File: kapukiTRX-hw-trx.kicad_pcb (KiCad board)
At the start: 4 copper layers, 45.7 x 27.9 mm, 97 parts, among them J1 GPS, J10 Conn_01x01, J11 Conn_01x01, J12 Conn_01x01, J13 Conn_01x01, J14 Conn_01x01, J15 Conn_01x01, J16 Conn_01x01, J17 Conn_01x01, J18 Conn_01x01, J19 GND for the Servo connectors, J2 SWD, J20 CAN, J21 Conn_01x01, J22 Conn_01x01, J3 Conn_01x01, J4 Conn_01x01, J5 Conn_01x01, J6 Conn_01x01, J7 Conn_01x01, J8 Conn_01x01, J9 Conn_01x01, U1 STM32G474VE, U2 LP38693-3.3, U3 TXB0108PWR, U4 LP38693-5.0, U5 MCP2562-E-MF, U6 LP38693SD-3.3, U7 BNO055, U8 BMP388, Y1 16MHz, Y2 32.768kHz

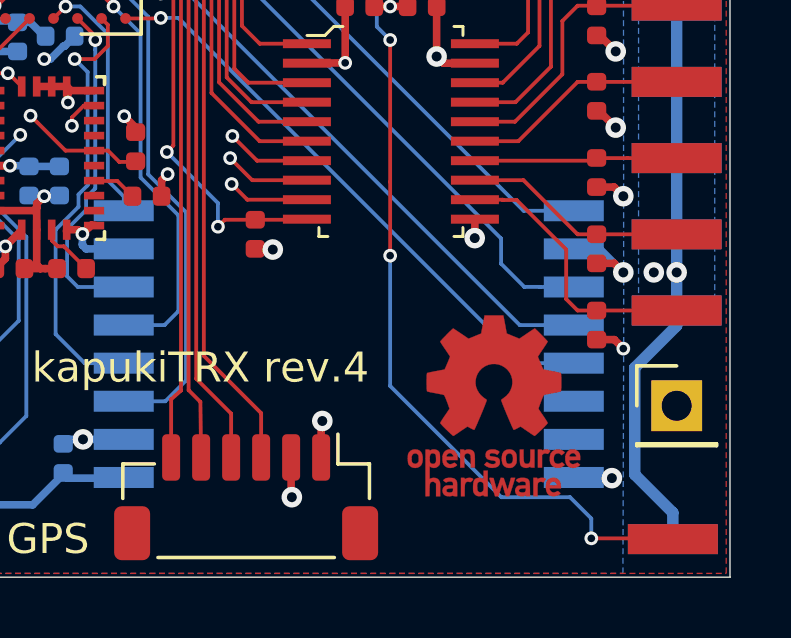
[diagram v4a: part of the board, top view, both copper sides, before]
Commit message: Add pull-up for uart
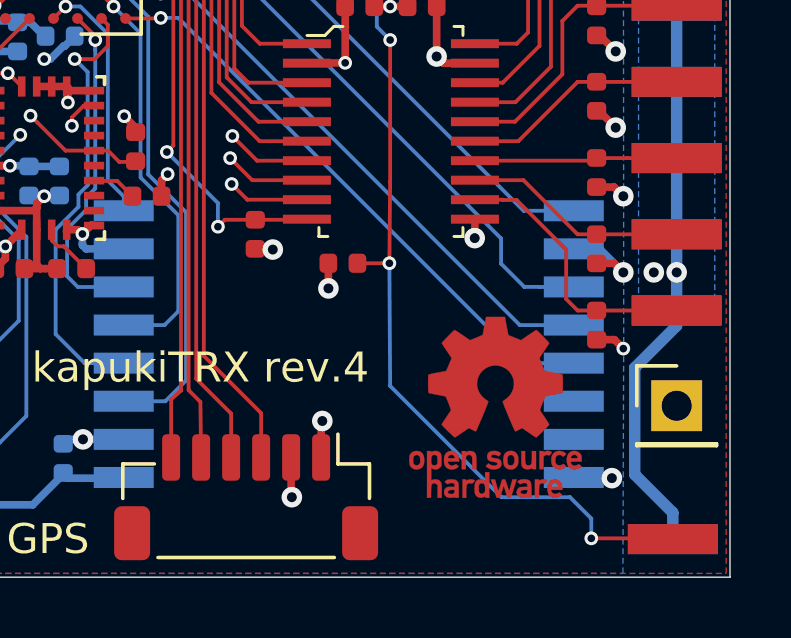
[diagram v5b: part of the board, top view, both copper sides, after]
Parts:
- added R19: 4k7, Resistor_SMD:R_0402_1005Metric, F.Cu at (204.3, 111.5)
- R16: value 10k -> 5k97
- R17: value 10k -> 2k4
- R6: value 1k -> 470
- R9: value 120R -> 120
- moved REF** 0.07 mm to (209.3, 116.3)
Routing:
- net /RXTX: track 42.2 -> 43.3 mm
- net /VCCCPU: track 49.8 -> 50.6 mm, vias 18 -> 19
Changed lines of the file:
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@@
-(kicad_pcb (version 20171130) (host pcbnew "(5.1.4)-1")
+(kicad_pcb (version 20171130) (host pcbnew "(5.1.4-0-10_14)")
   (general
     (thickness 1.6)
     (drawings 17)
-    (tracks 1089)
+    (tracks 1094)
     (zones 0)
-    (modules 97)
+    (modules 98)
     (nets 129)
   )
@@
   (layers
     (0 F.Cu signal)
-    (1 In1.Cu signal)
-    (2 In2.Cu signal)
-    (31 B.Cu signal)
+    (1 In1.Cu signal hide)
+    (2 In2.Cu signal hide)
+    (31 B.Cu signal hide)
     (32 B.Adhes user hide)
     (33 F.Adhes user hide)
@@
   )
   (module Symbol:OSHW-Logo_5.7x6mm_Copper (layer F.Cu)
-    (at 209.296 116.205)
+    (at 209.3468 116.2558)
     (descr "Open Source Hardware Logo")
     (tags "Logo OSHW")
@@
       (xy -1.971615 1.454739) (xy -1.908759 1.469184)) (layer F.Cu) (width 0.01))
   )
+  (module Resistor_SMD:R_0402_1005Metric (layer F.Cu)
+    (at 204.2668 111.4552 180)
+    (descr "Resistor SMD 0402 (1005 Metric), square (rectangular) end terminal, IPC_7351 nominal, (Body size source: http://www.tortai-tech.com/upload/download/2011102023233369053.pdf), generated with kicad-footprint-generator")
+    (tags resistor)
+    (attr smd)
+    (fp_text reference R19 (at 0 -1.17) (layer F.SilkS) hide
+      (effects (font (size 1 1) (thickness 0.15)))
+    )
+    (fp_text value 4k7 (at 0 1.17) (layer F.Fab)
+      (effects (font (size 1 1) (thickness 0.15)))
+    )
+    (fp_text user %R (at 0 0) (layer F.Fab)
+      (effects (font (size 0.25 0.25) (thickness 0.04)))
+    )
+    (fp_line (start 0.93 0.47) (end -0.93 0.47) (layer F.CrtYd) (width 0.05))
+    (fp_line (start 0.93 -0.47) (end 0.93 0.47) (layer F.CrtYd) (width 0.05))
+    (fp_line (start -0.93 -0.47) (end 0.93 -0.47) (layer F.CrtYd) (width 0.05))
+    (fp_line (start -0.93 0.47) (end -0.93 -0.47) (layer F.CrtYd) (width 0.05))
+    (fp_line (start 0.5 0.25) (end -0.5 0.25) (layer F.Fab) (width 0.1))
+    (fp_line (start 0.5 -0.25) (end 0.5 0.25) (layer F.Fab) (width 0.1))
+    (fp_line (start -0.5 -0.25) (end 0.5 -0.25) (layer F.Fab) (width 0.1))
+    (fp_line (start -0.5 0.25) (end -0.5 -0.25) (layer F.Fab) (width 0.1))
+    (pad 2 smd roundrect (at 0.485 0 180) (size 0.59 0.64) (layers F.Cu F.Paste F.Mask) (roundrect_rratio 0.25)
+      (net 25 /VCCCPU))
+    (pad 1 smd roundrect (at -0.485 0 180) (size 0.59 0.64) (layers F.Cu F.Paste F.Mask) (roundrect_rratio 0.25)
+      (net 122 /RXTX))
+    (model ${KISYS3DMOD}/Resistor_SMD.3dshapes/R_0402_1005Metric.wrl
+      (at (xyz 0 0 0))
+      (scale (xyz 1 1 1))
+      (rotate (xyz 0 0 0))
+    )
+  )
   (module Resistor_SMD:R_0402_1005Metric (layer B.Cu)
     (at 193.167 96.2152 180)
@@
       (effects (font (size 1 1) (thickness 0.15)))
     )
-    (fp_text value 10k (at 0 1.17) (layer F.Fab)
+    (fp_text value 2k4 (at 0 1.17) (layer F.Fab)
       (effects (font (size 1 1) (thickness 0.15)))
     )
@@
       (effects (font (size 1 1) (thickness 0.15)))
     )
-    (fp_text value 10k (at 0 1.17) (layer F.Fab)
+    (fp_text value 5k97 (at 0 1.17) (layer F.Fab)
       (effects (font (size 1 1) (thickness 0.15)))
     )
@@
       (effects (font (size 1 1) (thickness 0.15)))
     )
-    (fp_text value 1k (at 0 1.17) (layer F.Fab)
+    (fp_text value 470 (at 0 1.17) (layer F.Fab)
       (effects (font (size 1 1) (thickness 0.15)))
     )
@@
       (effects (font (size 1 1) (thickness 0.15)))
     )
-    (fp_text value 120R (at 0 1.17 90) (layer F.Fab)
+    (fp_text value 120 (at 0 1.17 90) (layer F.Fab)
       (effects (font (size 1 1) (thickness 0.15)))
     )
@@
   (segment (start 193.012211 97.686) (end 193.424417 98.098206) (width 0.254) (layer B.Cu) (net 25))
   (segment (start 192.7352 97.686) (end 193.012211 97.686) (width 0.254) (layer B.Cu) (net 25))
+  (via (at 203.7842 112.2934) (size 0.6858) (drill 0.3302) (layers F.Cu B.Cu) (net 25))
+  (segment (start 203.7818 112.291) (end 203.7842 112.2934) (width 0.254) (layer F.Cu) (net 25))
+  (segment (start 203.7818 111.4552) (end 203.7818 112.291) (width 0.254) (layer F.Cu) (net 25))
   (segment (start 178.435 115.339) (end 179.682 115.339) (width 0.381) (layer F.Cu) (net 26))
   (segment (start 179.635 115.113338) (end 179.940338 114.808) (width 0.381) (layer F.Cu) (net 26))
@@
   (segment (start 201.3458 95.2452) (end 201.3506 95.25) (width 0.127) (layer F.Cu) (net 122))
   (via (at 205.8416 104.013) (size 0.4572) (drill 0.254) (layers F.Cu B.Cu) (net 122))
-  (segment (start 205.8416 108.743222) (end 205.8416 104.013) (width 0.127) (layer F.Cu) (net 122))
   (via (at 195.7705 97.3328) (size 0.4572) (drill 0.254) (layers F.Cu B.Cu) (net 122))
   (segment (start 195.421 97.695) (end 195.421 97.6823) (width 0.127) (layer F.Cu) (net 122))
@@
   (segment (start 195.7705 97.3328) (end 197.1929 95.9104) (width 0.127) (layer In2.Cu) (net 122))
   (segment (start 201.3458 95.9104) (end 201.3458 95.25) (width 0.127) (layer F.Cu) (net 122))
-  (via (at 205.8416 111.2012) (size 0.4572) (drill 0.254) (layers F.Cu B.Cu) (net 122))
-  (segment (start 205.8416 108.743222) (end 205.8416 111.2012) (width 0.127) (layer F.Cu) (net 122))
   (via (at 212.5472 120.6246) (size 0.4572) (drill 0.254) (layers F.Cu B.Cu) (net 122))
   (segment (start 215.2396 120.6246) (end 215.265 120.65) (width 0.127) (layer F.Cu) (net 122))
@@
   (segment (start 205.397099 103.568499) (end 205.397099 97.424237) (width 0.127) (layer B.Cu) (net 122))
   (segment (start 205.8416 104.013) (end 205.397099 103.568499) (width 0.127) (layer B.Cu) (net 122))
+  (segment (start 205.5876 111.4552) (end 204.7518 111.4552) (width 0.127) (layer F.Cu) (net 122))
+  (segment (start 205.8162 111.4552) (end 205.5876 111.4552) (width 0.127) (layer F.Cu) (net 122))
   (segment (start 212.5472 119.9642) (end 212.5472 120.6246) (width 0.127) (layer B.Cu) (net 122))
   (segment (start 211.836 119.253) (end 212.5472 119.9642) (width 0.127) (layer B.Cu) (net 122))
   (segment (start 209.55 119.253) (end 211.836 119.253) (width 0.127) (layer B.Cu) (net 122))
-  (segment (start 205.8416 111.2012) (end 205.8416 115.5446) (width 0.127) (layer B.Cu) (net 122))
   (segment (start 205.8416 115.5446) (end 209.55 119.253) (width 0.127) (layer B.Cu) (net 122))
+  (segment (start 205.8162 111.4552) (end 205.8416 115.5446) (width 0.127) (layer B.Cu) (net 122))
+  (segment (start 205.8416 108.743222) (end 205.8416 104.013) (width 0.127) (layer F.Cu) (net 122))
+  (segment (start 205.8162 111.4552) (end 205.8416 108.743222) (width 0.127) (layer F.Cu) (net 122))
+  (via (at 205.8162 111.4552) (size 0.4572) (drill 0.254) (layers F.Cu B.Cu) (net 122))
   (via (at 194.9958 97.3074) (size 0.4572) (drill 0.254) (layers F.Cu B.Cu) (net 123))
   (segment (start 194.621 97.695) (end 194.621 97.6822) (width 0.127) (layer F.Cu) (net 123))

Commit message: rev.4 sent to JLCPCB
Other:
- board text added: "2014"
- board text added: "JLCJLCJLCJLC"
- board text removed: "2001"
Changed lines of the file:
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@@
   (general
     (thickness 1.6)
-    (drawings 17)
+    (drawings 18)
     (tracks 1094)
     (zones 0)
@@
     (34 B.Paste user hide)
     (35 F.Paste user hide)
-    (36 B.SilkS user hide)
+    (36 B.SilkS user)
     (37 F.SilkS user)
     (38 B.Mask user hide)
@@
     (pcbplotparams
       (layerselection 0x010fc_ffffffff)
-      (usegerberextensions false)
+      (usegerberextensions true)
       (usegerberattributes false)
       (usegerberadvancedattributes false)
@@
     )
   )
+  (gr_text JLCJLCJLCJLC (at 180.848 95.504 180) (layer B.SilkS)
+    (effects (font (size 1 1) (thickness 0.15)) (justify mirror))
+  )
   (gr_circle (center 178.181 98.3234) (end 178.2064 98.3742) (layer F.SilkS) (width 0.12))
   (gr_text P (at 210.185 120.904) (layer In2.Cu)
@@
     (effects (font (size 1.5 1.5) (thickness 0.3)))
   )
-  (gr_text "kapukiTRX rev.4" (at 199.517 114.935) (layer F.SilkS)
+  (gr_text "kapukiTRX rev.4" (at 199.517 114.554) (layer F.SilkS)
     (effects (font (size 1 1) (thickness 0.15)))
   )
-  (gr_text 2001 (at 186.563 120.65) (layer F.SilkS)
+  (gr_text 2014 (at 174.244 120.65) (layer F.SilkS)
     (effects (font (size 1 1) (thickness 0.15)))
   )

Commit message: Make some value changes for consistency
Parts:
- R16: value 5k97 -> 5k97 0.1%
- R17: value 2k4 -> 2k4 0.1%
- U6: value LP38693SD-3.3 -> LP38693-3.3
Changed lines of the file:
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@@
-(kicad_pcb (version 20171130) (host pcbnew "(5.1.4-0-10_14)")
+(kicad_pcb (version 20171130) (host pcbnew "(5.1.5)-3")
   (general
     (thickness 1.6)
@@
     (1 In1.Cu signal hide)
     (2 In2.Cu signal hide)
-    (31 B.Cu signal hide)
+    (31 B.Cu signal)
     (32 B.Adhes user hide)
     (33 F.Adhes user hide)
@@
       (effects (font (size 1 1) (thickness 0.15)))
     )
-    (fp_text value 2k4 (at 0 1.17) (layer F.Fab)
+    (fp_text value "2k4 0.1%" (at 0 1.17) (layer F.Fab)
       (effects (font (size 1 1) (thickness 0.15)))
     )
@@
       (effects (font (size 1 1) (thickness 0.15)))
     )
-    (fp_text value 5k97 (at 0 1.17) (layer F.Fab)
+    (fp_text value "5k97 0.1%" (at 0 1.17) (layer F.Fab)
       (effects (font (size 1 1) (thickness 0.15)))
     )
@@
       (effects (font (size 1 1) (thickness 0.15)))
     )
-    (fp_text value LP38693SD-3.3 (at 0 2.575) (layer F.Fab)
+    (fp_text value LP38693-3.3 (at 0 2.575) (layer F.Fab)
       (effects (font (size 1 1) (thickness 0.15)))
     )

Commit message: Remove R18 from silk
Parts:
- C33, C34, C37, C38: value 100n -> 100nF
- C35: value 6n8 -> 6.8nF
- C36: value 120n -> 120nF
- C39, C40: value 22p -> 22pF
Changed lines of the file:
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@@
     (tags resistor)
     (attr smd)
-    (fp_text reference R18 (at 0 1.17) (layer B.SilkS)
+    (fp_text reference R18 (at 0 1.17) (layer B.SilkS) hide
       (effects (font (size 1 1) (thickness 0.15)) (justify mirror))
     )
@@
       (effects (font (size 1 1) (thickness 0.15)))
     )
-    (fp_text value 22p (at 0 1.17 90) (layer F.Fab)
+    (fp_text value 22pF (at 0 1.17 90) (layer F.Fab)
       (effects (font (size 1 1) (thickness 0.15)))
     )
@@
       (effects (font (size 1 1) (thickness 0.15)))
     )
-    (fp_text value 22p (at 0 1.17) (layer F.Fab)
+    (fp_text value 22pF (at 0 1.17) (layer F.Fab)
       (effects (font (size 1 1) (thickness 0.15)))
     )
@@
       (effects (font (size 1 1) (thickness 0.15)))
     )
-    (fp_text value 100n (at 0 1.17) (layer F.Fab)
+    (fp_text value 100nF (at 0 1.17) (layer F.Fab)
       (effects (font (size 1 1) (thickness 0.15)))
     )
@@
       (effects (font (size 1 1) (thickness 0.15)))
     )
-    (fp_text value 100n (at 0 1.17) (layer F.Fab)
+    (fp_text value 100nF (at 0 1.17) (layer F.Fab)
       (effects (font (size 1 1) (thickness 0.15)))
     )
@@
       (effects (font (size 1 1) (thickness 0.15)) (justify mirror))
     )
-    (fp_text value 120n (at 0 -1.17 270) (layer B.Fab)
+    (fp_text value 120nF (at 0 -1.17 270) (layer B.Fab)
       (effects (font (size 1 1) (thickness 0.15)) (justify mirror))
     )
@@
       (effects (font (size 1 1) (thickness 0.15)) (justify mirror))
     )
-    (fp_text value 6n8 (at 0 -1.17 270) (layer B.Fab)
+    (fp_text value 6.8nF (at 0 -1.17 270) (layer B.Fab)
       (effects (font (size 1 1) (thickness 0.15)) (justify mirror))
     )
@@
       (effects (font (size 1 1) (thickness 0.15)))
     )
-    (fp_text value 100n (at 0 1.17) (layer F.Fab)
+    (fp_text value 100nF (at 0 1.17) (layer F.Fab)
       (effects (font (size 1 1) (thickness 0.15)))
     )
@@
       (effects (font (size 1 1) (thickness 0.15)))
     )
-    (fp_text value 100n (at 0 1.17 90) (layer F.Fab)
-      (effects (font (size 1 1) (thickness 0.15)))
-    )
+    (fp_text value 100nF (at 0 1.17 90) (layer F.Fab)
+      (effects (font (size 1 1) (thickness 0.15)))
+    )
